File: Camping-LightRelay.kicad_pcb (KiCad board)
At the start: 2 copper layers, 43 x 63 mm, 90 parts, among them CN1 U262-061N-4BVC11, CN2 907-152A1022D10200, CN3 907-152A1022D10200, CN5 B2B-XH-A, J1 PH2.54-07-04PWD, J4 J300, Q1 FDV301N, Q2 BC817, Q3 IRF7404, Q4 BC847, U1 USBLC6-2SC6, U2 CD4011UBM, U3 SI1865DDL, U5 TLC555DTR, U6 LMV358ID

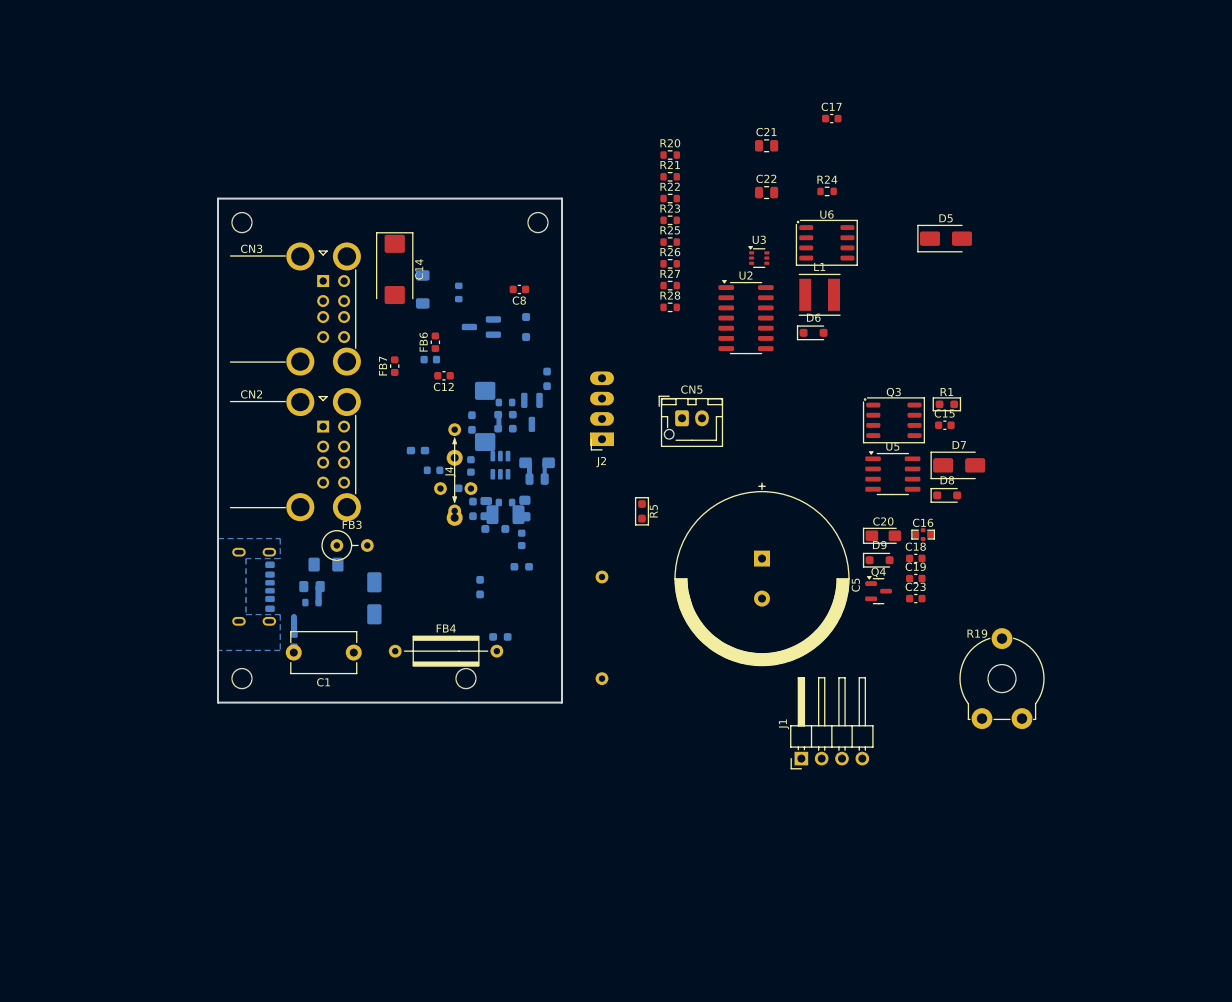
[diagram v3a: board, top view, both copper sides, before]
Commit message: Переход на 2-х стороннюю ПП
Топология ПП выбрана двусторонняя в виду миниатюрности устройства. Изменение посадочных мест под новую топологию.
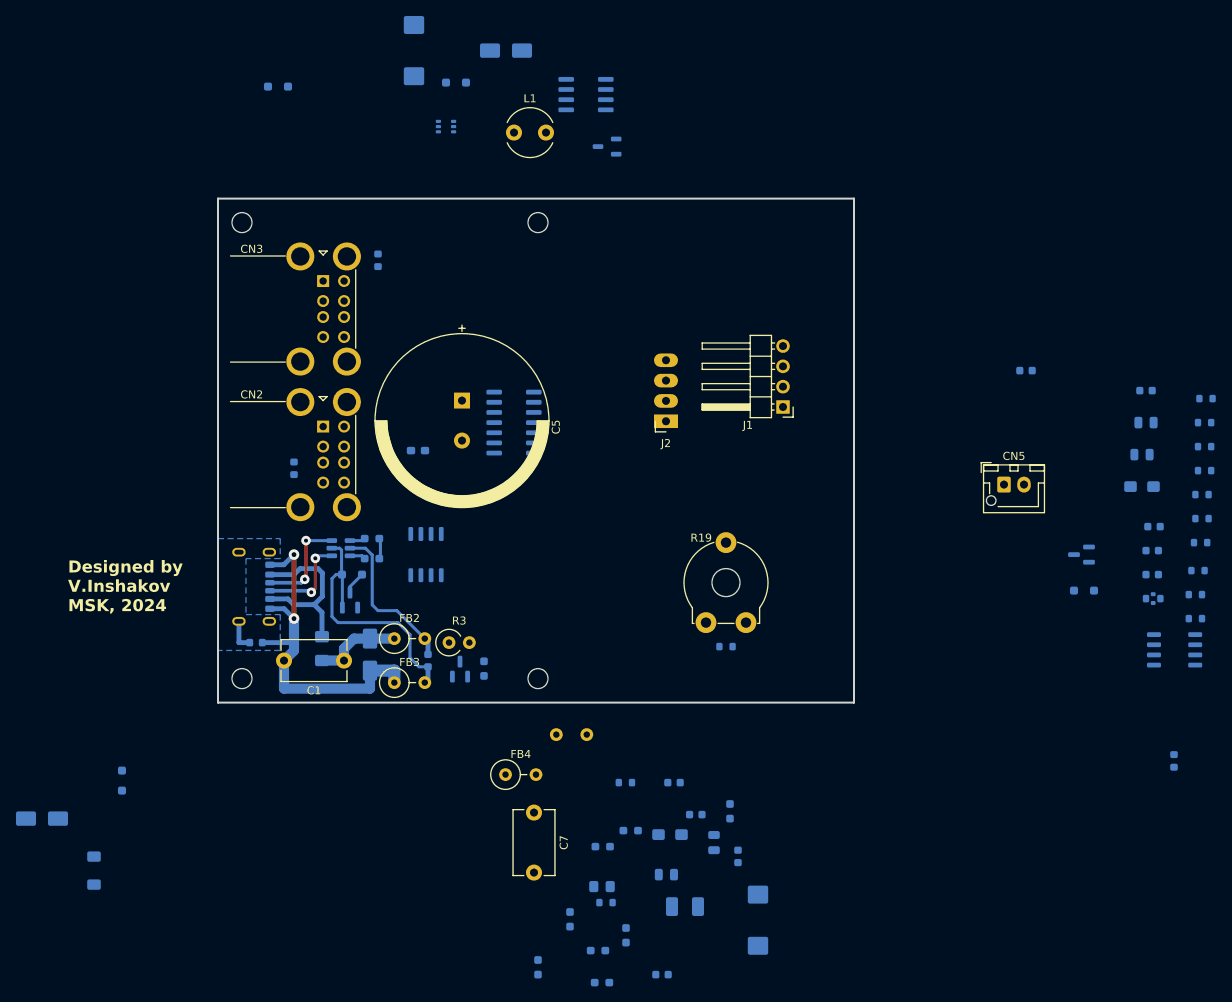
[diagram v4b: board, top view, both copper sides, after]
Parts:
- removed J4: J300, lib:Junction_400mil
- added U4: ME2108A50M, Package_TO_SOT_SMD:SOT-23-3, B.Cu at (127.6, 36.5)
- C12, C14, C15, C16, C17, C18, C19, C20, C21, C22, C23, C8, D5, D6, D7, D8, D9, FB6, FB7, Q3, Q4, R1, R20, R21, R22, R23, R24, R25, R26, R27, R28, R5, U2, U3, U5, U6: moved to B.Cu
- C7: moved to F.Cu
- FB2: footprint PCM_Ferrite_THT_AKL:Ferrite_L8.0mm_D3.5mm_P12.70mm -> PCM_Ferrite_THT_AKL:Ferrite_L8.0mm_D3.5mm_P3.81mm_Vertical; moved to F.Cu
- FB4: footprint PCM_Ferrite_THT_AKL:Ferrite_L8.0mm_D3.5mm_P12.70mm -> PCM_Ferrite_THT_AKL:Ferrite_L8.0mm_D3.5mm_P3.81mm_Vertical
- L1: footprint Inductor_SMD:L_Taiyo-Yuden_NR-50xx -> Inductor_THT:L_Radial_D6.0mm_P4.00mm
- Q1, Q2: footprint PCM_Package_TO_SOT_SMD_AKL:SOT-23_BigPads -> Package_TO_SOT_SMD:SOT-23
- R3: value 42 -> 43; footprint PCM_Resistor_SMD_AKL:R_0805_2012Metric_Pad1.15x1.40mm -> Resistor_THT:R_Axial_DIN0309_L9.0mm_D3.2mm_P2.54mm_Vertical; moved to F.Cu
- moved D5 134.3 mm to (57.0, 120.5), turned to 180 degrees
- moved FB8 99.4 mm to (198.5, 113.3), turned to 90 degrees
- moved D8 98.0 mm to (86.5, 29.0), turned to 180 degrees
- moved R18 94.3 mm to (202.5, 68.0), turned to 180 degrees
- moved R20 87.6 mm to (201.2, 95.5), turned to 180 degrees
- moved R21 83.9 mm to (201.2, 92.5), turned to 180 degrees
- moved D4 83.5 mm to (63.5, 127.0)
- moved R22 80.7 mm to (201.5, 89.5), turned to 180 degrees
- moved R23 77.6 mm to (201.8, 86.0), turned to 180 degrees
- moved C15 77.2 mm to (134.5, 140.0), turned to 180 degrees
- moved D7 76.8 mm to (115.0, 24.5), turned to 180 degrees
- moved D3 75.9 mm to (67.0, 115.8)
- moved R25 74.9 mm to (202.0, 83.0), turned to 180 degrees
- moved R1 73.8 mm to (98.2, 85.5)
- moved R26 72.5 mm to (202.0, 80.0), turned to 180 degrees
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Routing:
- net Net-(D1-A2): track 2.15 -> 46.3 mm, vias 0 -> 2
- net GNDE: track 0.00 -> 33.4 mm
- net Net-(CN1-VBUS-PadA9): track 0.00 -> 21.7 mm
- net Net-(D3-A): track 0.00 -> 20.1 mm
- net Net-(CN1-CC2): track 0.00 -> 12.7 mm, vias 0 -> 2
- net Net-(CN1-CC1): track 0.00 -> 11.9 mm, vias 0 -> 2
- net Net-(D1-A1): track 0.00 -> 11.1 mm
- net Net-(D2-A1): track 0.00 -> 5.49 mm
- net (no net): track 4.03 -> 0.00 mm
- net /SH-NET: track 0.00 -> 4.00 mm
- net GND: track 2.03 -> 0.00 mm
- net Net-(R2-Pad1): track 0.00 -> 1.98 mm
- net Net-(R1-Pad1): track 0.00 -> 1.94 mm
- net Net-(Q2-C): track 1.74 -> 0.00 mm
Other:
- board size 43 x 63 mm -> 79.5 x 63 mm
- board text added: "Designed by V.Inshakov MSK, 2024"

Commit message: Разводка ПП, трассировка, оптимизация
Отказ от идеи с субмодулем, все разводится на двухсторонней ПП.
Вынос аналогового фотореле на отдельный лист схемы.
Разводка двусторонней ПП
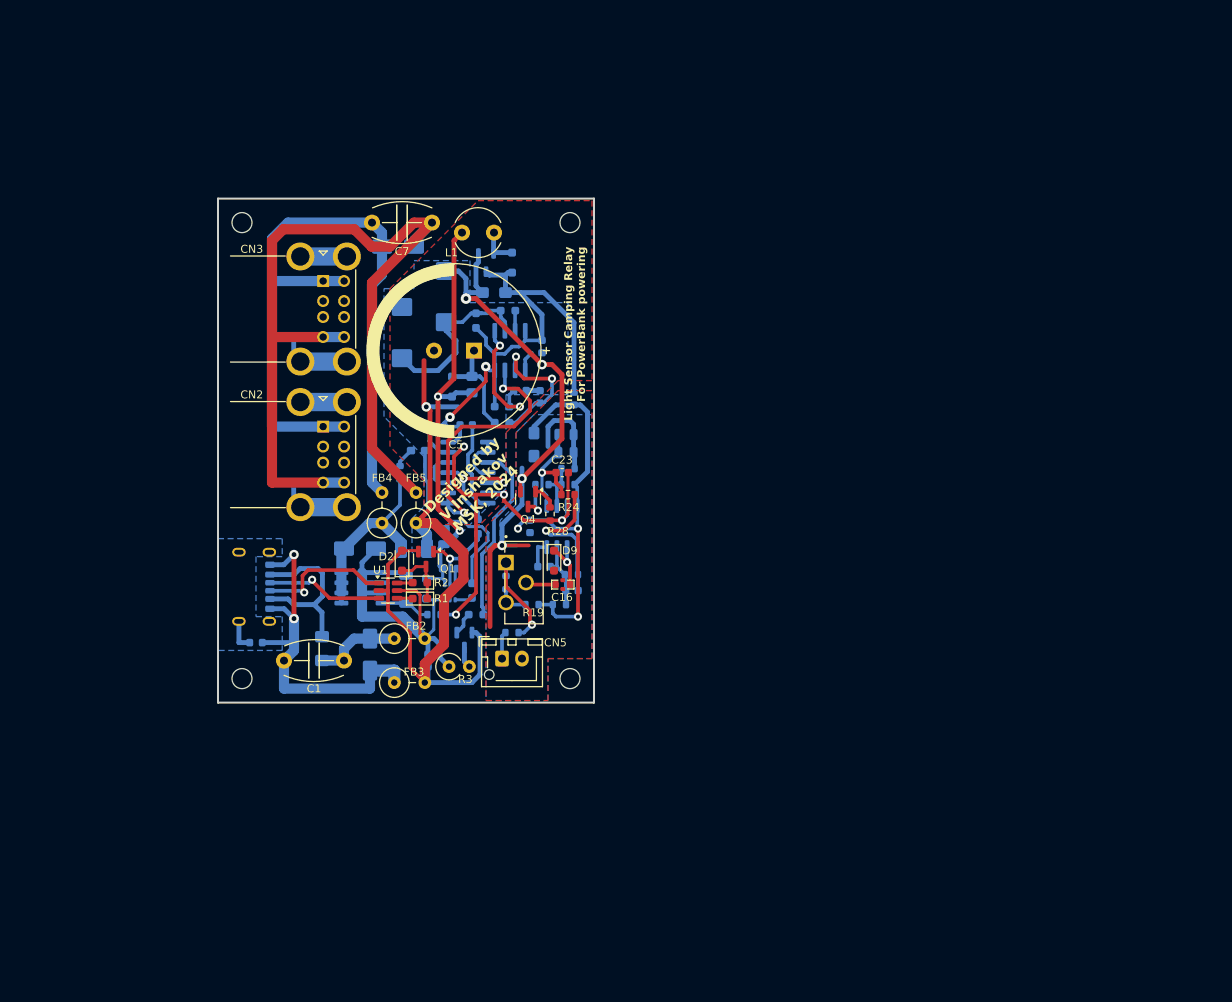
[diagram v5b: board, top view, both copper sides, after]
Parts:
- removed C10: 1uF, Capacitor_SMD:C_0805_2012Metric
- removed C12: 0.1, Capacitor_SMD:C_0603_1608Metric
- removed J1: PH2.54-07-04PWD, Connector_PinHeader_2.54mm:PinHeader_1x04_P2.54mm_Horizontal
- removed J2: ~, lib:PinSolder_1x04_P2.54mm
- removed R22: 100k 1%, Resistor_SMD:R_0603_1608Metric
- C1, C7: footprint Capacitor_THT:C_Disc_D8.0mm_W5.0mm_P7.50mm -> PCM_Capacitor_THT_AKL:C_Disc_D7.5mm_W5.0mm_P7.50mm
- C16, C23, D2, D9, FB5, Q1, Q4, R1, R2, R24, R28, U1: moved to F.Cu
- R19: footprint lib:Potentiometer_Bochen_PT10 -> lib:TRIM_PTN10-A01HB20
- moved R18 88.1 mm to (118.2, 93.8)
- moved FB8 87.6 mm to (123.5, 68.0), turned to -90 degrees
- moved C13 85.9 mm to (102.0, 59.8)
- moved R20 85.4 mm to (115.8, 97.2)
- moved R27 82.8 mm to (119.5, 78.8)
- moved R28 82.3 mm to (120.5, 82.4), turned to -90 degrees
- moved R15 80.2 mm to (111.2, 58.2), turned to -90 degrees
- moved R24 80.1 mm to (122.8, 80.0)
- moved R21 79.5 mm to (121.7, 93.8), turned to 0 degrees
- moved R14 79.5 mm to (115.2, 57.0), turned to 180 degrees
- moved R25 79.4 mm to (122.8, 78.8)
- moved R26 79.3 mm to (122.8, 76.8), turned to 0 degrees
- moved R23 78.8 mm to (123.2, 90.0), turned to 0 degrees
- moved U6 78.1 mm to (122.0, 84.0), turned to 90 degrees
- moved C19 78.0 mm to (118.0, 84.0), turned to -90 degrees
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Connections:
- C11 pad 1: GND2 -> GNDE
- C16 pad 2: GND -> GNDE
- C17 pad 2: GND -> GNDE
- C19 pad 2: GND -> GNDE
- C20 pad 2: GND -> GNDE
- C21 pad 2: GND -> GNDE
- C22 pad 2: GND -> GNDE
- C23 pad 2: /Субмодуль фотореле/~{RELAY_ON} -> /~{LOAD_ON}
- CN5 pad 2: GND -> GNDE
- D9 pad 2: GND -> GNDE
- FB8 pad 1: /Субмодуль фотореле/+5V -> VCC
- Q4 pad 2: GND -> GNDE
- R26 pad 2: GND -> GNDE
- R28 pad 2: /Субмодуль фотореле/~{RELAY_ON} -> /~{LOAD_ON}
- U6 pad 4: GND -> GNDE
- U6 pad 7: /Субмодуль фотореле/~{RELAY_ON} -> /~{LOAD_ON}
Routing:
- net GNDE: track 33.4 -> 222.2 mm, vias 0 -> 5
- net Net-(CN2-GND1): track 0.00 -> 118.4 mm
- net Net-(CN2-VBUS1): track 0.00 -> 90.2 mm
- net VCC: track 0.00 -> 66.6 mm, vias 0 -> 2
- net /~{LOAD_ON}: track 0.00 -> 56.5 mm, vias 0 -> 4
- net Net-(D3-K): track 0.00 -> 54.3 mm, vias 0 -> 2
- net Net-(U6.1-V+): track 0.00 -> 50.1 mm, vias 0 -> 3
- net Net-(D3-A): track 20.1 -> 53.9 mm
- net Net-(U5-Q): track 0.00 -> 33.3 mm, vias 0 -> 2
- net Net-(D5-A2): track 0.00 -> 23.6 mm
- net Net-(U5-THR): track 0.00 -> 23.6 mm
- net Net-(R4-Pad1): track 0.00 -> 22.8 mm
- net Net-(C18-Pad2): track 0.00 -> 18.1 mm, vias 0 -> 1
- net Net-(U5-TR): track 0.00 -> 17.2 mm, vias 0 -> 2
- net Net-(CN3-Shield): track 0.00 -> 16.6 mm
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- added copper zone on B.Cu, net GNDE
- added copper zone on F.Cu, net GNDE
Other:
- board size 79.5 x 63 mm -> 47 x 63 mm
- board text added: "Light Sensor Camping Relay For PowerBank powering"

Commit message: Доделка ПП до финала
Проверка DRC, подгонка автоправил трассирования дорожек. Корректировка технических ограничений ПП. Расчет номиналов конденсаторов C11, C12.
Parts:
- added R22: 100k 1%, Resistor_SMD:R_0603_1608Metric, B.Cu at (122.5, 96.2)
- C11: renamed from C13; value 680uFx6.3V -> 470uFx6.3V; footprint Capacitor_Tantalum_SMD:CP_EIA-7343-43_Kemet-X_Pad2.25x2.55mm_HandSolder -> Capacitor_Tantalum_SMD:CP_EIA-7343-31_Kemet-D_Pad2.25x2.55mm_HandSolder
- C12: renamed from C14; value 680uFx6.3V -> 470uFx6.3V; footprint Capacitor_Tantalum_SMD:CP_EIA-7343-43_Kemet-X_Pad2.25x2.55mm_HandSolder -> Capacitor_Tantalum_SMD:CP_EIA-7343-31_Kemet-D_Pad2.25x2.55mm_HandSolder
- renumbered C11 to C10, C15 to C13, C16 to C14, C17 to C15, C18 to C16, C19 to C17, C20 to C18, C21 to C19, C22 to C20, C23 to C21
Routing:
- net GNDE: track 222.2 -> 210.4 mm, vias 5 -> 22
- net Net-(U6.1-+): track 8.49 -> 10.2 mm
- net Net-(U6.1-V+): track 50.1 -> 51.7 mm

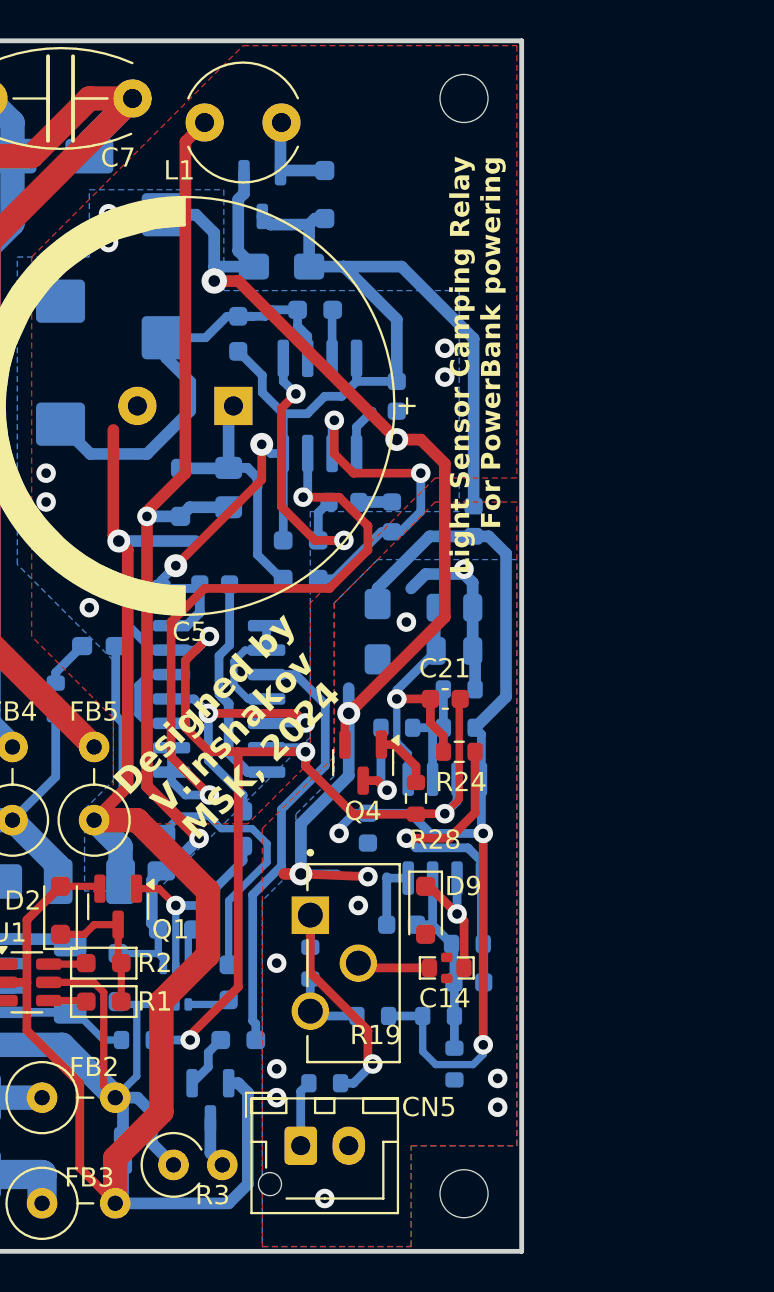
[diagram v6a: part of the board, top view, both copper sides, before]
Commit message: Первая сборка production
Сборка всей конструкции и проверка на ПП, проверка работы
* Правка посадочного места ионистор C3 и печатной платы для него
* Замена D3 на обычный 1N4148 из-за утечек Шоттки
* Замена стабилитрона D4 на двойной TVS-диод, т.к. обнаружился обходной ток от внутреннего DC/DC преобразователя
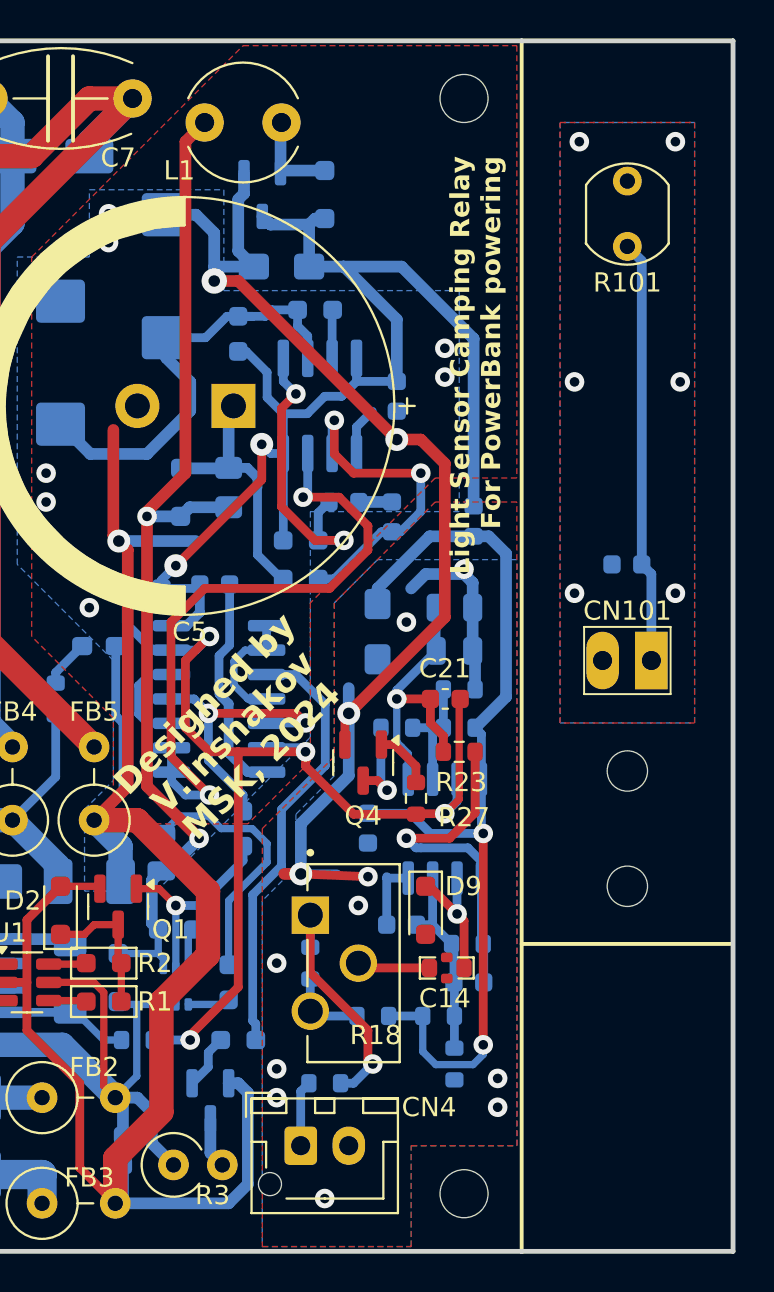
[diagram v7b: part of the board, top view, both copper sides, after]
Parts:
- added C101: 1n, Capacitor_SMD:C_0603_1608Metric, B.Cu at (131.5, 70.2)
- added CN101: XHP-2, lib:PinSolder_1x2_P2.54mm, F.Cu at (132.8, 75.2)
- added HOLE101: MountingHole_2.1mm, MountingHole:MountingHole_2.1mm, F.Cu at (131.5, 87.0)
- added HOLE101: MountingHole_2.1mm, MountingHole:MountingHole_2.1mm, F.Cu at (131.5, 81.0)
- added R101: GL5516, OptoDevice:R_LDR_5.1x4.3mm_P3.4mm_Vertical, F.Cu at (131.5, 53.7)
- Q4: value BC847 -> BSS138
- R10: value 10k -> 470
- R7: value 2.2k -> 2.7k
- renumbered CN5 to CN4, R17 to R16, R18 to R17, R19 to R18, R20 to R19, R21 to R20, R22 to R21, R23 to R22, R24 to R23, R25 to R24, R26 to R25, R27 to R26, R28 to R27
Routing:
- net Net-(CN101-Pin_1): track 0.00 -> 22.1 mm
- net Net-(U6.1-V+): track 51.7 -> 49.6 mm, vias 3 -> 2
- net GND2: vias 0 -> 6
- added copper zone on B.Cu, net GND2
- added copper zone on F.Cu, net GND2
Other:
- board size 47 x 63 mm -> 58 x 63 mm
